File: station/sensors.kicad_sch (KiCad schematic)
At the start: 10 parts, among them J4 STEMMA, J5 RJ11, J6 RJ11, J7 DS18B20

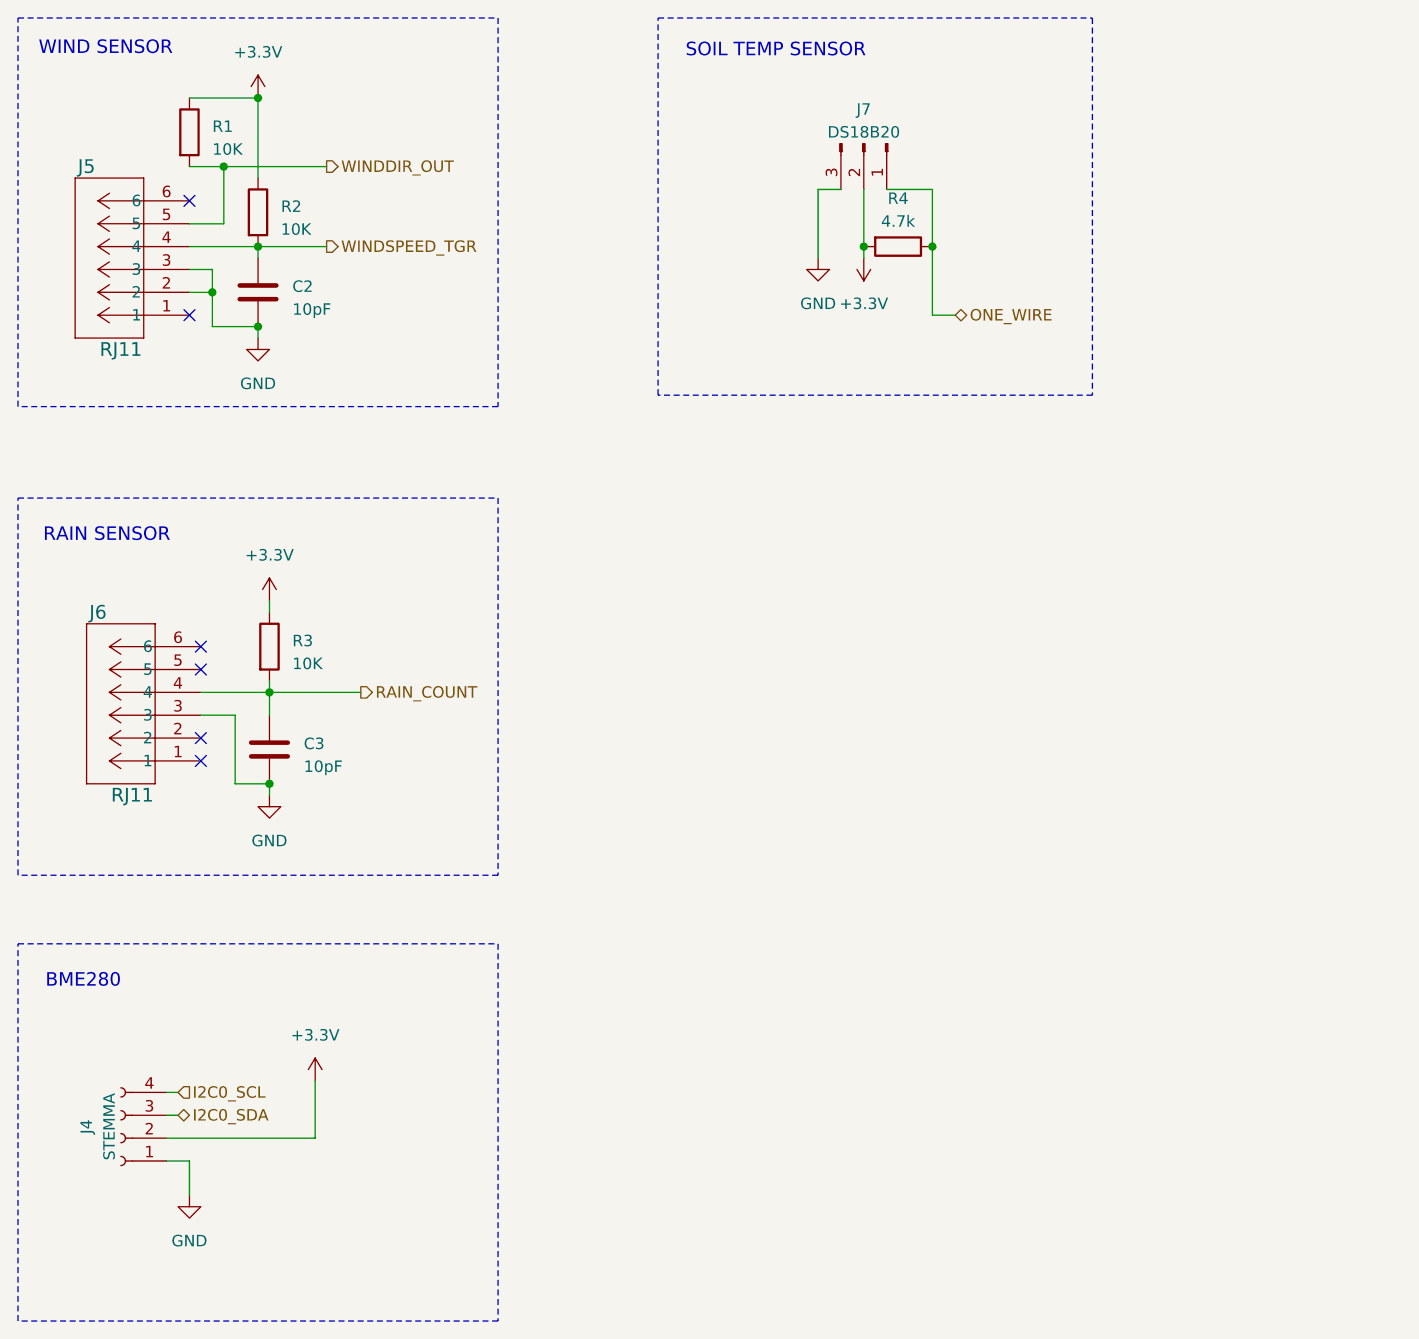
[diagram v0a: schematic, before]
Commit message: Reworked layout
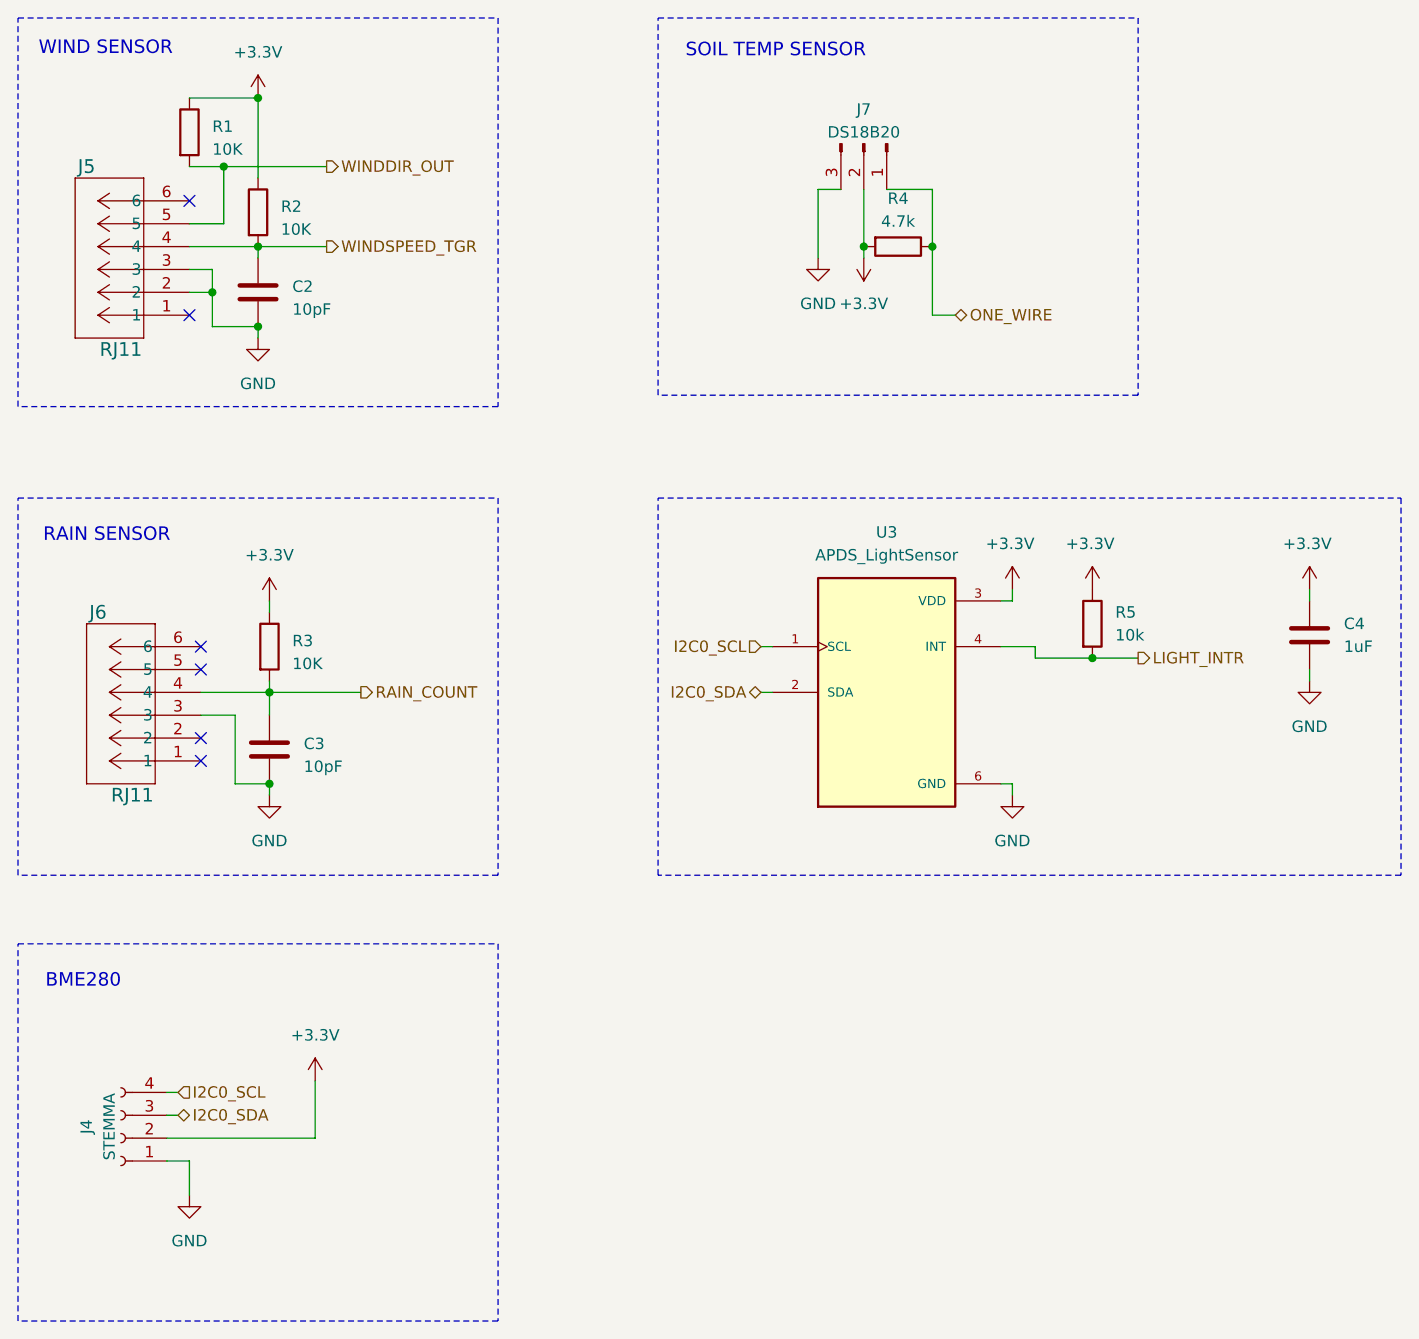
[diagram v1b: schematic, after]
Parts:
- added C4: 1uF, Capacitor_SMD:C_0805_2012Metric_Pad1.18x1.45mm_HandSolder, symbol Device:C
- added R5: 10k, Resistor_SMD:R_0805_2012Metric_Pad1.20x1.40mm_HandSolder, symbol Device:R
- added U3: APDS_LightSensor, WeatherStation:APDS_LIGHT_SENSOR, symbol Weather_Sensors:APDS_LightSensor
- J4: footprint WeatherStation:STEMMA_LARGE -> WeatherStation:STEMMA_SMALL
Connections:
- net +3.3V: now also C4.1, R5.1, U3.3 (VDD)
- net GND: now also C4.2, U3.6 (GND)
- net I2C0_SCL: now also U3.1 (SCL)
- net I2C0_SDA: now also U3.2 (SDA)
- new net LIGHT_INTR: R5.2, U3.4 (INT)

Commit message: Switched to a round board
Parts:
- added J7: SOIL_MOISTURE, WeatherStation:Stemma_Vertical_Large, symbol Connector:Conn_01x04_Socket
- J4: value STEMMA -> BME280; footprint WeatherStation:STEMMA_SMALL -> WeatherStation:StemmaQT_Vertical
- J5: value RJ11 -> WIND_SENSOR; footprint WeatherStation:CONN6_5555165-1_TEC -> WeatherStation:RJ11_SMD
- J6: value RJ11 -> RAIN_SENSOR; footprint WeatherStation:CONN6_5555165-1_TEC -> WeatherStation:RJ11_SMD
- J8: renamed from J7; value DS18B20 -> SOIL_TEMP; footprint WeatherStation:STEMMA_LARGE_3pin -> WeatherStation:Stemma_Vertical_Large
- U3: value APDS_LightSensor -> LIGHT_SENSOR
- renumbered R1 to R5, R2 to R6, R3 to R7, R4 to R8, R5 to R9
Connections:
- net +3.3V: now also J7.2 (Pin_2)
- net GND: now also J7.1 (Pin_1)
- net I2C0_SCL: now also J7.4 (Pin_4)
- net I2C0_SDA: now also J7.3 (Pin_3)
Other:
- note added: "SOIL MOISTURE"

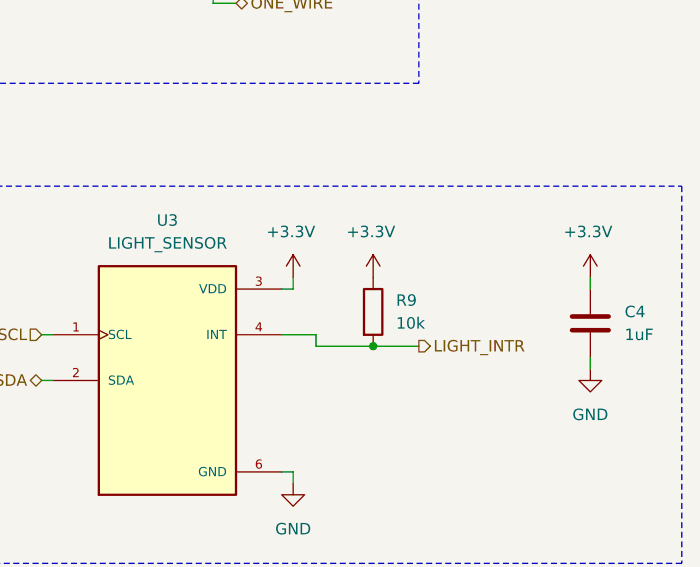
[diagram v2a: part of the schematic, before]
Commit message: Finished Square layout
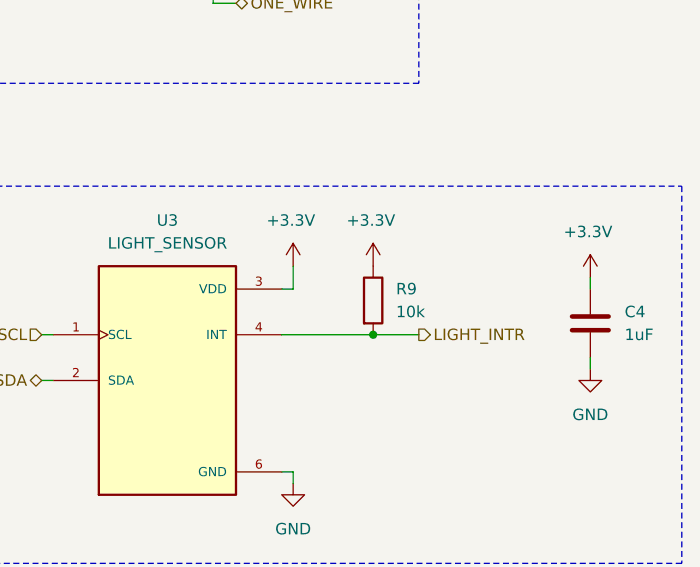
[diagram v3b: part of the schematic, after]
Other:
- moved on the sheet: R9
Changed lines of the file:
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@@
-	)
-	(junction
-		(at 144.78 95.25)
-		(diameter 0)
-		(color 0 0 0 0)
 	)
 	(junction
@@
 	)
 	(junction
+		(at 144.78 93.98)
+		(diameter 0)
+		(color 0 0 0 0)
+	)
+	(junction
 		(at 53.34 99.06)
 		(diameter 0)
@@
 	(wire
 		(pts
-			(xy 144.78 95.25) (xy 149.86 95.25)
+			(xy 144.78 93.98) (xy 149.86 93.98)
 		)
 		(stroke
@@
 	(wire
 		(pts
-			(xy 138.43 93.98) (xy 138.43 95.25)
-		)
-		(stroke
-			(width 0)
-			(type default)
-		)
-	)
-	(wire
-		(pts
 			(xy 127 43.18) (xy 127 49.53)
 		)
@@
 	(wire
 		(pts
-			(xy 134.62 93.98) (xy 138.43 93.98)
+			(xy 134.62 93.98) (xy 144.78 93.98)
 		)
 		(stroke
@@
 	(wire
 		(pts
-			(xy 135.89 88.9) (xy 135.89 87.63)
+			(xy 135.89 86.36) (xy 135.89 88.9)
 		)
 		(stroke
@@
 		(pts
 			(xy 53.34 109.22) (xy 53.34 110.49)
-		)
-		(stroke
-			(width 0)
-			(type default)
-		)
-	)
-	(wire
-		(pts
-			(xy 138.43 95.25) (xy 144.78 95.25)
 		)
 		(stroke
@@
 	(hierarchical_label "LIGHT_INTR"
 		(shape output)
-		(at 149.86 95.25 0)
+		(at 149.86 93.98 0)
 		(fields_autoplaced yes)
 		(effects
@@
 	(symbol
 		(lib_id "Device:R")
-		(at 144.78 91.44 0)
+		(at 144.78 90.17 0)
 		(unit 1)
 		(exclude_from_sim no)
@@
 		(fields_autoplaced yes)
 		(property "Reference" "R9"
-			(at 147.32 90.1699 0)
+			(at 147.32 88.8999 0)
 			(effects
 				(font
@@
 		)
 		(property "Value" "10k"
-			(at 147.32 92.7099 0)
+			(at 147.32 91.4399 0)
 			(effects
 				(font
@@
 		)
 		(property "Footprint" "Resistor_SMD:R_0805_2012Metric_Pad1.20x1.40mm_HandSolder"
-			(at 143.002 91.44 90)
+			(at 143.002 90.17 90)
 			(effects
 				(font
@@
 		)
 		(property "Datasheet" "~"
-			(at 144.78 91.44 0)
+			(at 144.78 90.17 0)
 			(effects
 				(font
@@
 		)
 		(property "Description" "Resistor"
-			(at 144.78 91.44 0)
+			(at 144.78 90.17 0)
 			(effects
 				(font
@@
 	(symbol
 		(lib_id "power:VCC")
-		(at 135.89 87.63 0)
+		(at 135.89 86.36 0)
 		(unit 1)
 		(exclude_from_sim no)
@@
 		(dnp no)
 		(property "Reference" "#PWR028"
-			(at 135.89 91.44 0)
+			(at 135.89 90.17 0)
 			(effects
 				(font
@@
 		)
 		(property "Value" "+3.3V"
-			(at 135.636 82.55 0)
+			(at 135.636 81.28 0)
 			(effects
 				(font
@@
 		)
 		(property "Footprint" ""
-			(at 135.89 87.63 0)
+			(at 135.89 86.36 0)
 			(effects
 				(font
@@
 		)
 		(property "Datasheet" ""
-			(at 135.89 87.63 0)
+			(at 135.89 86.36 0)
 			(effects
 				(font
@@
 		)
 		(property "Description" ""
-			(at 135.89 87.63 0)
+			(at 135.89 86.36 0)
 			(effects
 				(font
@@
 	(symbol
 		(lib_id "power:VCC")
-		(at 144.78 87.63 0)
+		(at 144.78 86.36 0)
 		(unit 1)
 		(exclude_from_sim no)
@@
 		(dnp no)
 		(property "Reference" "#PWR030"
-			(at 144.78 91.44 0)
+			(at 144.78 90.17 0)
 			(effects
 				(font
@@
 		)
 		(property "Value" "+3.3V"
-			(at 144.526 82.55 0)
+			(at 144.526 81.28 0)
 			(effects
 				(font
@@
 		)
 		(property "Footprint" ""
-			(at 144.78 87.63 0)
+			(at 144.78 86.36 0)
 			(effects
 				(font
@@
 		)
 		(property "Datasheet" ""
-			(at 144.78 87.63 0)
+			(at 144.78 86.36 0)
 			(effects
 				(font
@@
 		)
 		(property "Description" ""
-			(at 144.78 87.63 0)
-			(effects
-				(font
+			(at 144.78 86.36 0)
+			(effects
+				(font

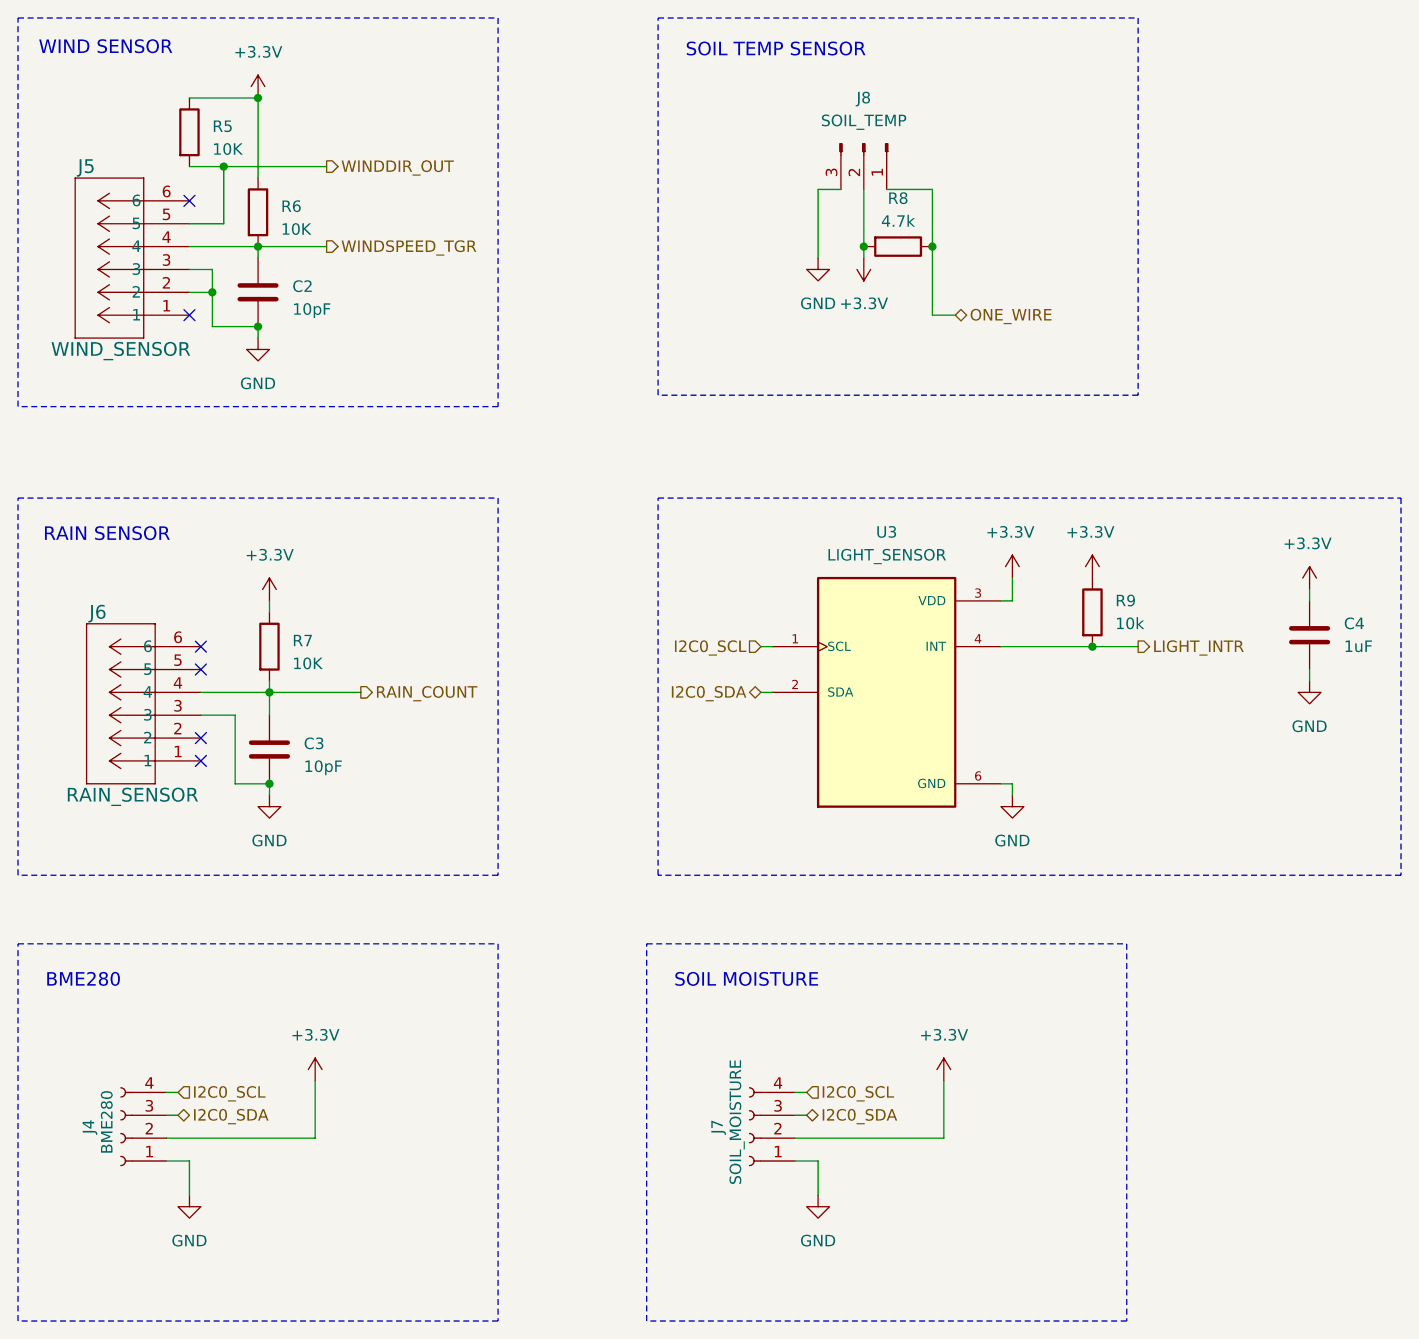
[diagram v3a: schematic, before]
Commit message: Updated the I2C schematic for the soil moisture sensor
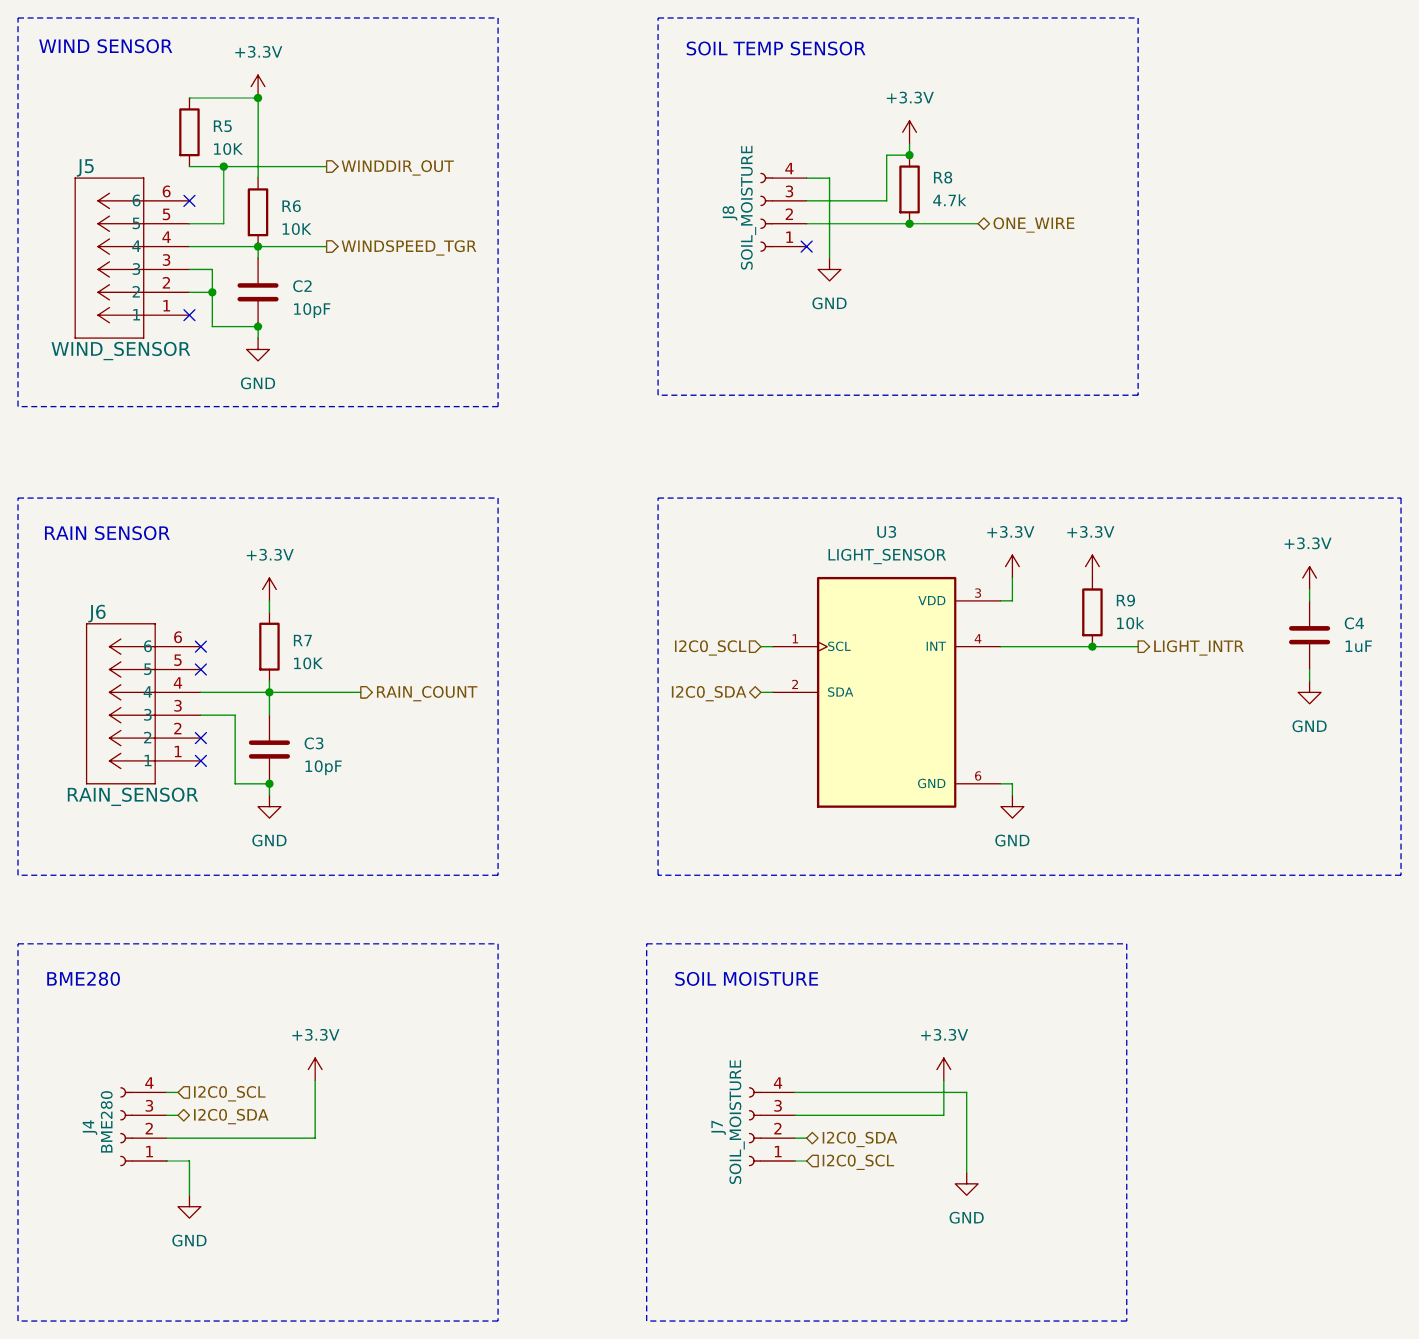
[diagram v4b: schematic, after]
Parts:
- removed J8: SOIL_TEMP, WeatherStation:Stemma_Vertical_Large, symbol Connector:Conn_01x03_Pin
- added J8: SOIL_MOISTURE, WeatherStation:Stemma_Vertical_Large, symbol Connector:Conn_01x04_Socket
- R8: footprint Resistor_SMD:R_0805_2012Metric_Pad1.20x1.40mm_HandSolder -> (none)
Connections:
- net +3.3V: now also J7.3 (Pin_3), R8.1, J8.3 (Pin_3); no longer J7.2 (Pin_2), R8.2
- net GND: now also J7.4 (Pin_4), J8.4 (Pin_4); no longer J7.1 (Pin_1)
- net I2C0_SCL: now also J7.1 (Pin_1); no longer J7.4 (Pin_4)
- net I2C0_SDA: now also J7.2 (Pin_2); no longer J7.3 (Pin_3)
- net ONE_WIRE: now also R8.2, J8.2 (Pin_2); no longer R8.1
- no-connect marks 6 -> 7
